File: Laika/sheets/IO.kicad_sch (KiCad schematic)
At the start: 0 parts

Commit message: Added external GPIO's for user use
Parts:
- added J9: Conn_01x07, symbol Connector_Generic:Conn_01x07
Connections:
- new net +1V8: J9.1 (Pin_1)
- new net GND: J9.7 (Pin_7)
- new net IO_ADC1: J9.6 (Pin_6)
- new net IO_GPIOB_22: J9.2 (Pin_2)
- new net IO_PWM10: J9.3 (Pin_3)
- new net IO_PWM12: J9.4 (Pin_4)
- new net IO_PWM13: J9.5 (Pin_5)
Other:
- note added: "IO Breakout"
- note added: "PWM and IO"
- note added: "The PWM and ADC pins can also function as GPIO's"
- note added: "These signals are all 1.8V logic level. Require a external level shifter if you want 3.3V"

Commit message: Populated BOM with part numbers and footprints
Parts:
- J9: footprint (none) -> Connector_PinHeader_1.00mm:PinHeader_1x07_P1.00mm_Vertical
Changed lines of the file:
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@@
 			)
 		)
-		(property "Footprint" ""
+		(property "Footprint" "Connector_PinHeader_1.00mm:PinHeader_1x07_P1.00mm_Vertical"
 			(at 151.13 93.98 0)
 			(effects

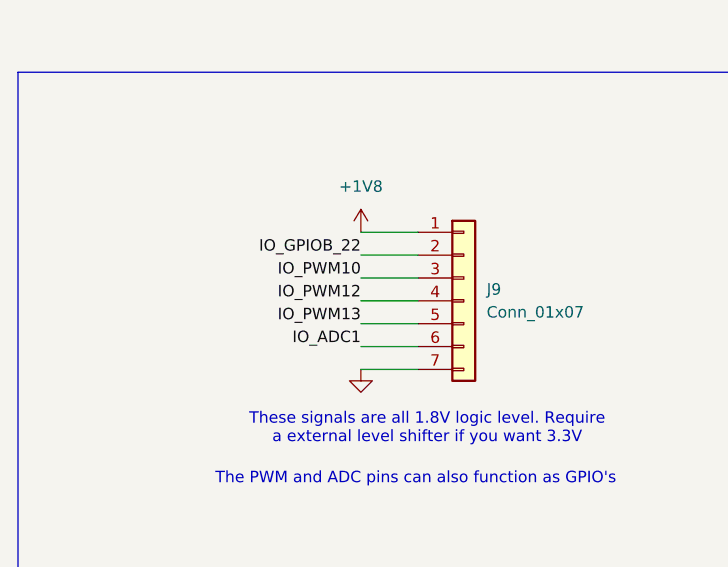
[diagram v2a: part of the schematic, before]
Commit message: Rearranged external IO pins
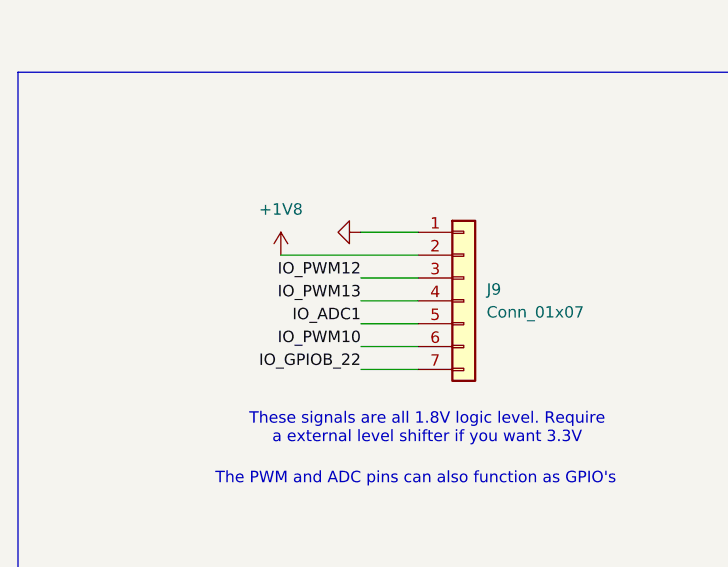
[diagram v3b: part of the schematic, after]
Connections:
- net +1V8: now also J9.2 (Pin_2); no longer J9.1 (Pin_1)
- net GND: now also J9.1 (Pin_1); no longer J9.7 (Pin_7)
- net IO_ADC1: now also J9.5 (Pin_5); no longer J9.6 (Pin_6)
- net IO_GPIOB_22: now also J9.7 (Pin_7); no longer J9.2 (Pin_2)
- net IO_PWM10: now also J9.6 (Pin_6); no longer J9.3 (Pin_3)
- net IO_PWM12: now also J9.3 (Pin_3); no longer J9.4 (Pin_4)
- net IO_PWM13: now also J9.4 (Pin_4); no longer J9.5 (Pin_5)
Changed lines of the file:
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@@
 	(wire
 		(pts
-			(xy 139.7 88.9) (xy 146.05 88.9)
+			(xy 130.81 88.9) (xy 146.05 88.9)
 		)
 		(stroke
@@
 		)
 	)
+	(label "IO_ADC1"
+		(at 139.7 96.52 180)
+		(effects
+			(font
+				(size 1.27 1.27)
+			)
+			(justify right bottom)
+		)
+	)
+	(label "IO_PWM12"
+		(at 139.7 91.44 180)
+		(effects
+			(font
+				(size 1.27 1.27)
+			)
+			(justify right bottom)
+		)
+	)
 	(label "IO_PWM10"
-		(at 139.7 91.44 180)
+		(at 139.7 99.06 180)
 		(effects
 			(font
@@
 	)
 	(label "IO_PWM13"
-		(at 139.7 96.52 180)
+		(at 139.7 93.98 180)
 		(effects
 			(font
@@
 	)
 	(label "IO_GPIOB_22"
-		(at 139.7 88.9 180)
-		(effects
-			(font
-				(size 1.27 1.27)
-			)
-			(justify right bottom)
-		)
-	)
-	(label "IO_PWM12"
-		(at 139.7 93.98 180)
-		(effects
-			(font
-				(size 1.27 1.27)
-			)
-			(justify right bottom)
-		)
-	)
-	(label "IO_ADC1"
-		(at 139.7 99.06 180)
+		(at 139.7 101.6 180)
 		(effects
 			(font
@@
 	(symbol
 		(lib_id "power:GND")
-		(at 139.7 101.6 0)
+		(at 139.7 86.36 270)
 		(unit 1)
 		(exclude_from_sim no)
@@
 		(fields_autoplaced yes)
 		(property "Reference" "#PWR0105"
-			(at 139.7 107.95 0)
+			(at 133.35 86.36 0)
 			(effects
 				(font
@@
 		)
 		(property "Value" "GND"
-			(at 139.7 106.68 0)
+			(at 134.62 86.36 0)
 			(effects
 				(font
@@
 		)
 		(property "Footprint" ""
-			(at 139.7 101.6 0)
+			(at 139.7 86.36 0)
 			(effects
 				(font
@@
 		)
 		(property "Datasheet" ""
-			(at 139.7 101.6 0)
+			(at 139.7 86.36 0)
 			(effects
 				(font
@@
 		)
 		(property "Description" "Power symbol creates a global label with name \"GND\" , ground"
-			(at 139.7 101.6 0)
+			(at 139.7 86.36 0)
 			(effects
 				(font
@@
 	(symbol
 		(lib_id "power:+1V8")
-		(at 139.7 86.36 0)
+		(at 130.81 88.9 0)
 		(unit 1)
 		(exclude_from_sim no)
@@
 		(fields_autoplaced yes)
 		(property "Reference" "#PWR0106"
-			(at 139.7 90.17 0)
+			(at 130.81 92.71 0)
 			(effects
 				(font
@@
 		)
 		(property "Value" "+1V8"
-			(at 139.7 81.28 0)
+			(at 130.81 83.82 0)
 			(effects
 				(font
@@
 		)
 		(property "Footprint" ""
-			(at 139.7 86.36 0)
+			(at 130.81 88.9 0)
 			(effects
 				(font
@@
 		)
 		(property "Datasheet" ""
-			(at 139.7 86.36 0)
+			(at 130.81 88.9 0)
 			(effects
 				(font
@@
 		)
 		(property "Description" "Power symbol creates a global label with name \"+1V8\""
-			(at 139.7 86.36 0)
+			(at 130.81 88.9 0)
 			(effects
 				(font
@@
 		)
 		(instances
-			(project ""
+			(project "Laika"
 				(path "/57baccbf-5d29-4714-8f2e-7e9f593fcdf8/6c078d98-f795-4bff-ba6d-ace5d579e960/81224984-5643-4c36-ac79-8e44b8e923a5"
 					(reference "#PWR0106")
